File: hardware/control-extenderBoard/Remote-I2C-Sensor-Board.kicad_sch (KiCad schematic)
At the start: 21 parts, among them J16 12V + GND (TP), J19 3V3 + GND (TP), J20 SCL6 + GND (TP), J21 SDA6 + GND (TP), U13 AS5600_Breakout, U14 PCA9600D

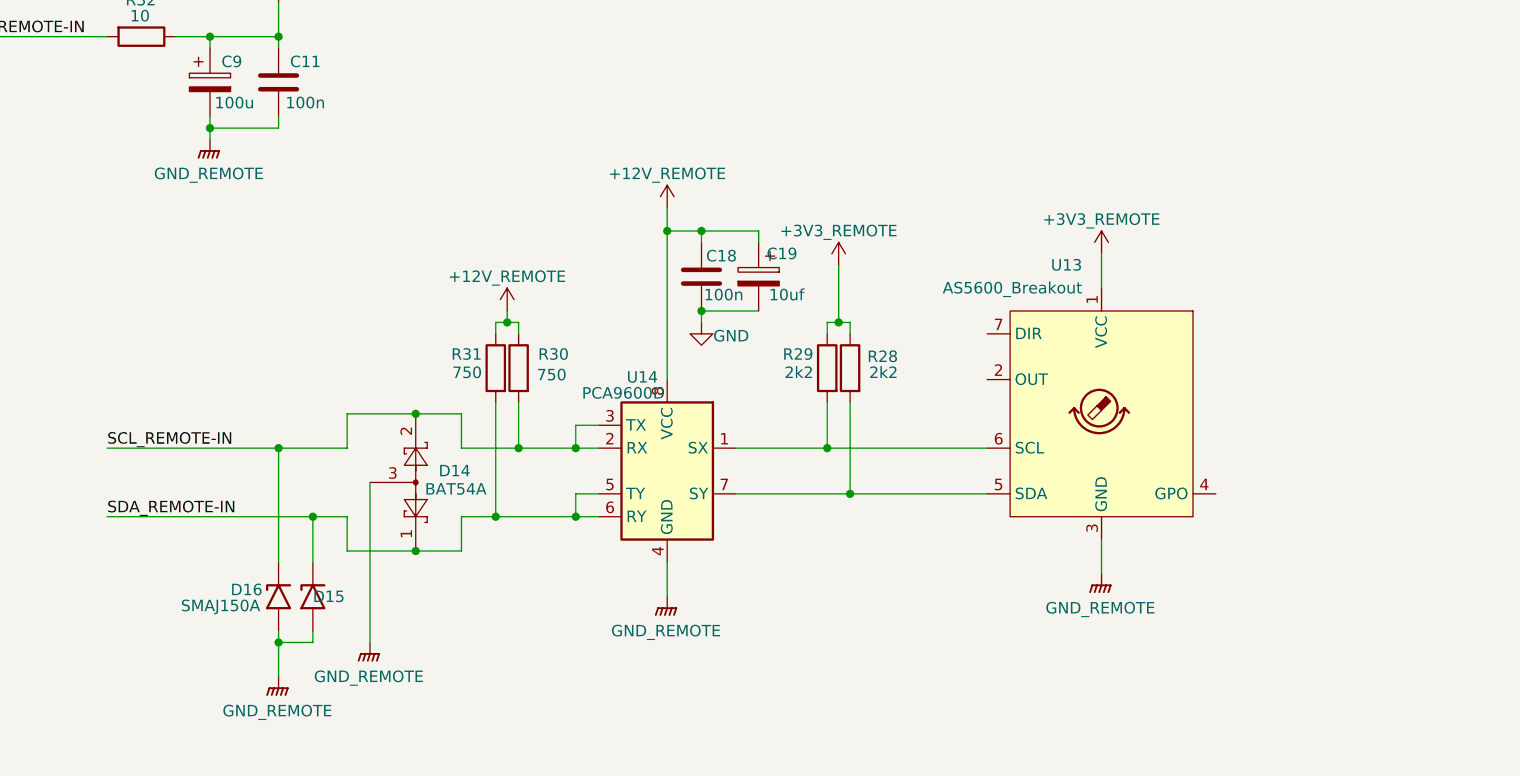
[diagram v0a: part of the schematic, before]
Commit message: extenderBoard: Evaluate part availability, Rework i2c protection
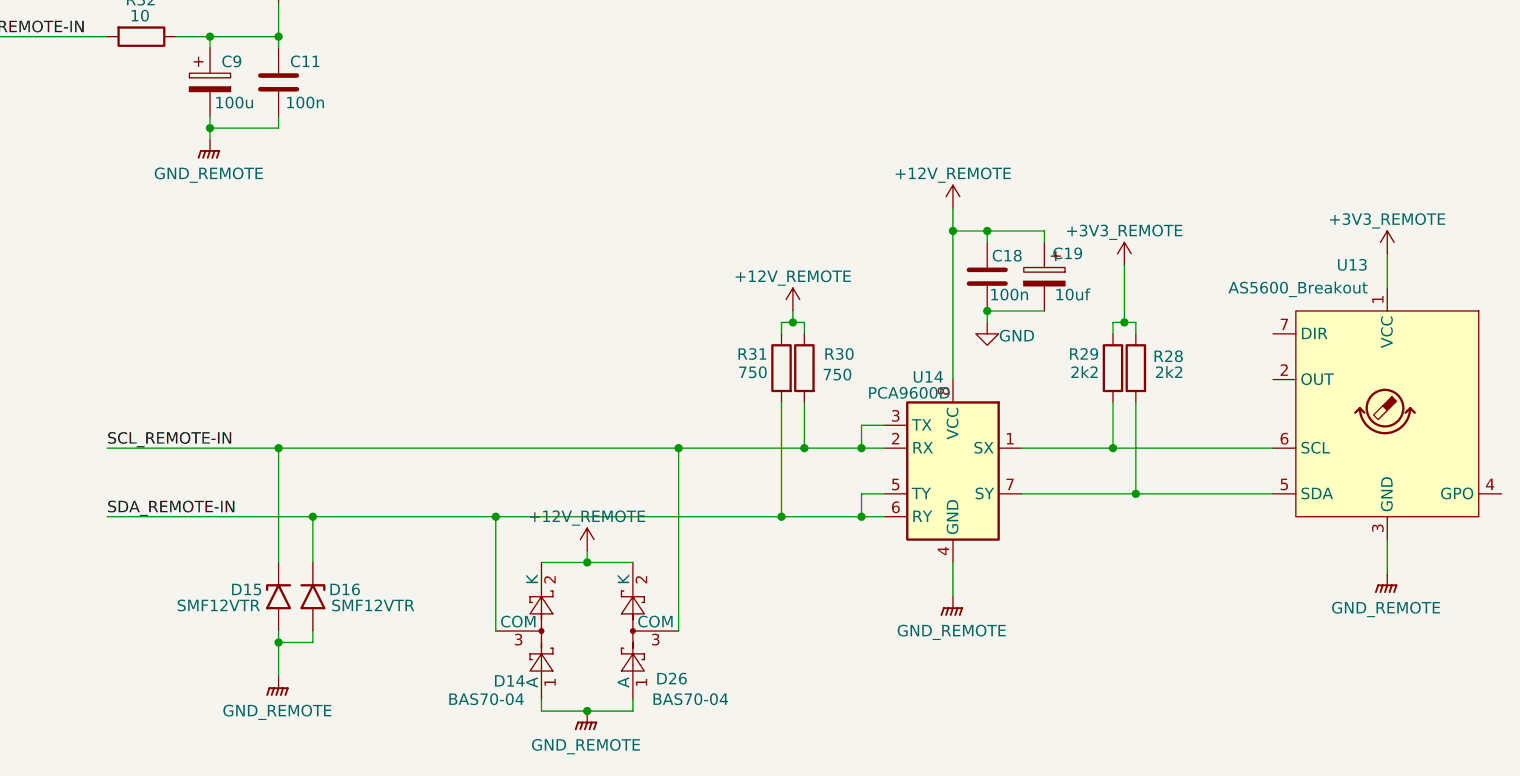
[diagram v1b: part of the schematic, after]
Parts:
- removed D14: BAT54A, Package_TO_SOT_SMD:SOT-23, symbol Diode:BAT54A
- added D14, D26: BAS70-04, Package_TO_SOT_SMD:SOT-23-3, symbol Diode:BAT54SW
- C9: footprint Capacitor_THT:CP_Radial_D8.0mm_P5.00mm -> Capacitor_THT:CP_Radial_D6.3mm_P2.50mm
- D15, D16: value SMAJ150A -> SMF12VTR; footprint Diode_SMD:D_SMA -> Diode_SMD:D_SOD-123F
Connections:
- net +12V_REMOTE: now also D14.2 (K), D26.2 (K)
- net GND_REMOTE: now also D14.1 (A), D26.1 (A)
- net SCL_REMOTE-IN: now also D15.1 (A1), D26.3 (COM); no longer D16.1 (A1)
- net SDA_REMOTE-IN: now also D16.1 (A1), D14.3 (COM); no longer D15.1 (A1)
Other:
- moved on the sheet: C18, C19, R28, R29, R30, R31, U13, U14

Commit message: extenderBoard: Route RS485, I2C reserve, Add Testpoints, GND-Zones
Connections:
- net GND is gone; now on net GND_REMOTE: C18.2, C19.2
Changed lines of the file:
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@@
+	)
+	(symbol
+		(lib_id "power:GNDPWR")
+		(at 195.58 82.55 0)
+		(unit 1)
+		(exclude_from_sim no)
+		(in_bom yes)
+		(on_board yes)
+		(dnp no)
+		(fields_autoplaced yes)
+		(property "Reference" "#PWR098"
+			(at 195.58 87.63 0)
+			(effects
+				(font
+					(size 1.27 1.27)
+				)
+				(hide yes)
+			)
+		)
+		(property "Value" "GND_REMOTE"
+			(at 195.453 86.36 0)
+			(effects
+				(font
+					(size 1.27 1.27)
+				)
+			)
+		)
+		(property "Footprint" ""
+			(at 195.58 83.82 0)
+			(effects
+				(font
+					(size 1.27 1.27)
+				)
+				(hide yes)
+			)
+		)
+		(property "Datasheet" ""
+			(at 195.58 83.82 0)
+			(effects
+				(font
+					(size 1.27 1.27)
+				)
+				(hide yes)
+			)
+		)
+		(property "Description" "Power symbol creates a global label with name \"GNDPWR\" , global ground"
+			(at 195.58 82.55 0)
+			(effects
+				(font
+					(size 1.27 1.27)
+				)
+				(hide yes)
+			)
+		)
+		(pin "1"
+		)
+		(instances
+			(project "control-extenderBoard"
+				(path "/e3fc34d4-dad6-4201-965b-dc5b1bdae059/246abe15-ec2a-4d65-af0f-025db67f32a6"
+					(reference "#PWR098")
+					(unit 1)
+				)
+			)
+		)
 	)
 	(symbol
@@
 					(unit 1)
 				)
-			)
-		)
-	)
-	(symbol
-		(lib_id "power:GND")
-		(at 195.58 82.55 0)
-		(unit 1)
-		(exclude_from_sim no)
-		(in_bom yes)
-		(on_board yes)
-		(dnp no)
-		(property "Reference" "#PWR098"
-			(at 195.58 88.9 0)
-			(effects
-				(font
-					(size 1.27 1.27)
-				)
-				(hide yes)
-			)
-		)
-		(property "Value" "GND"
-			(at 198.882 84.074 0)
-			(effects
-				(font
-					(size 1.27 1.27)
-				)
-			)
-		)
-		(property "Footprint" ""
-			(at 195.58 82.55 0)
-			(effects
-				(font
-					(size 1.27 1.27)
-				)
-				(hide yes)
-			)
-		)
-		(property "Datasheet" ""
-			(at 195.58 82.55 0)
-			(effects
-				(font
-					(size 1.27 1.27)
-				)
-				(hide yes)
-			)
-		)
-		(property "Description" "Power symbol creates a global label with name \"GND\" , ground"
-			(at 195.58 82.55 0)
-			(effects
-				(font
-					(size 1.27 1.27)
-				)
-				(hide yes)
-			)
-		)
-		(pin "1"
-		)
-		(instances
-			(project "control-extenderBoard"
-				(path "/e3fc34d4-dad6-4201-965b-dc5b1bdae059/246abe15-ec2a-4d65-af0f-025db67f32a6"
-					(reference "#PWR098")
-					(unit 1)
-				)

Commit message: extenderBoard: Add pcb text, Arrange remote-board
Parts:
- added H5, H6, H7, H8: MountingHole_Pad, mountingHoles_libJonny:MountingHole_2.2mm_NPTH-with-pad_DRC-clearance-error, symbol Mechanical:MountingHole_Pad
- added J2: CAT6-Shield, misc_libJonny:Shield_Landing_Pad_6mmCable_ZipTie, symbol misc_libJonny:Shield_Landing_Pad
- added TP12: GND, Connector_PinHeader_2.54mm:PinHeader_1x01_P2.54mm_Vertical, symbol Connector:TestPoint
- added TP19: SCL, Connector_PinHeader_2.54mm:PinHeader_1x01_P2.54mm_Vertical, symbol Connector:TestPoint
- added TP20: 12V-Filtered, Connector_PinHeader_2.54mm:PinHeader_1x01_P2.54mm_Vertical, symbol Connector:TestPoint
- added TP21: 3V3-IN, Connector_PinHeader_2.54mm:PinHeader_1x01_P2.54mm_Vertical, symbol Connector:TestPoint
- added TP22: 3V3-Filtered, Connector_PinHeader_2.54mm:PinHeader_1x01_P2.54mm_Vertical, symbol Connector:TestPoint
- added TP23: SDA, Connector_PinHeader_2.54mm:PinHeader_1x01_P2.54mm_Vertical, symbol Connector:TestPoint
- added TP24: SCL-in, Connector_PinHeader_2.54mm:PinHeader_1x01_P2.54mm_Vertical, symbol Connector:TestPoint
- added TP25: SDA-in, Connector_PinHeader_2.54mm:PinHeader_1x01_P2.54mm_Vertical, symbol Connector:TestPoint
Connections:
- net +12V_REMOTE: now also TP20.1
- net +3V3_REMOTE: now also TP22.1
- net 3V3_REMOTE-IN: now also TP21.1
- net GND_REMOTE: now also H5.1, H6.1, H7.1, H8.1, TP12.1
- net SCL_REMOTE-IN: now also TP24.1
- net SDA_REMOTE-IN: now also TP25.1
- net at R29.2, U13.6 (SCL), U14.1 (SX): now also TP19.1
- net at R28.2, U13.5 (SDA), U14.7 (SY): now also TP23.1
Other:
- note added: "Cable mount"
- moved on the sheet: D14, D26

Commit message: extenderBoard: Route separate remote/sensor-board
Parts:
- removed J2: CAT6-Shield, misc_libJonny:Shield_Landing_Pad_6mmCable_ZipTie, symbol misc_libJonny:Shield_Landing_Pad
- added TP26: GND, Connector_PinHeader_2.54mm:PinHeader_1x01_P2.54mm_Vertical, symbol Connector:TestPoint
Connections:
- net GND_REMOTE: now also J20.2 (Pin_2), J21.2 (Pin_2), TP26.1; no longer J20.1 (Pin_1), J21.1 (Pin_1)
- net SCL_REMOTE-IN: now also J20.1 (Pin_1); no longer J20.2 (Pin_2)
- net SDA_REMOTE-IN: now also J21.1 (Pin_1); no longer J21.2 (Pin_2)
- net SCL_AS5600: now reaches R29.2, TP19.1, U13.6 (SCL), U14.1 (SX)
- net SDA_AS5600: now reaches R28.2, TP23.1, U13.5 (SDA), U14.7 (SY)
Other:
- note removed: "Cable mount"
- moved on the sheet: J20, J21, R28, R29

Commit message: extenderBoard: Add ferrite-beads, Swap 12V TVS diodes
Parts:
- removed D15, D16: SMF12VTR, Diode_SMD:D_SOD-123F, symbol Diode:SMAJ150A
- added D12, D16: PESD12VL1BA, Diode_SMD:D_SOD-123F, symbol Device:D_TVS
- added FB1, FB3: FerriteBead AWBC-09, Resistor_THT:R_Axial_DIN0614_L14.3mm_D5.7mm_P5.08mm_Vertical, symbol Device:FerriteBead
- R32, R33: footprint Resistor_THT:R_Axial_DIN0207_L6.3mm_D2.5mm_P10.16mm_Horizontal -> Resistor_THT:R_Axial_DIN0207_L6.3mm_D2.5mm_P2.54mm_Vertical
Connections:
- net 12V_REMOTE-IN: now also FB3.1; no longer R32.2
- net 3V3_REMOTE-IN: now also FB1.1; no longer R33.2
- net GND_REMOTE: now also D12.1 (A1), D16.1 (A1)
- net SCL_REMOTE-IN: now also D16.2 (A2)
- net SDA_REMOTE-IN: now also D12.2 (A2)
- new net: FB3.2, R32.2
- new net: FB1.2, R33.2
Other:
- moved on the sheet: C11, C12, C13, C9, R32, R33, TP20, TP21, TP22
